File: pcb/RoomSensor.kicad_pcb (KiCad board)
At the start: 2 copper layers, 82 x 36.5 mm, 75 parts, among them J1 FH34SRJ-24S-0.5SH50, J2 USB_C_Receptacle_PowerOnly_6P, J3 programming, J4 Conn_01x04_Pin, J5 Conn_01x04_Pin, J6 Conn_01x02_Pin, Q1 SI1308EDL-T1-GE3, Q2 AO3401A, Q3 ALS-PT19-315C/L177/TR8, SW1 SW_Push, U1 ESP32-WROOM-32D, U2 DW01-P, U3 CEG8205A, U4 RT9080-33GJ5, U5 TP4056, U6 SCD40-D-R1, U7 SHT31-DIS, U8 BME680

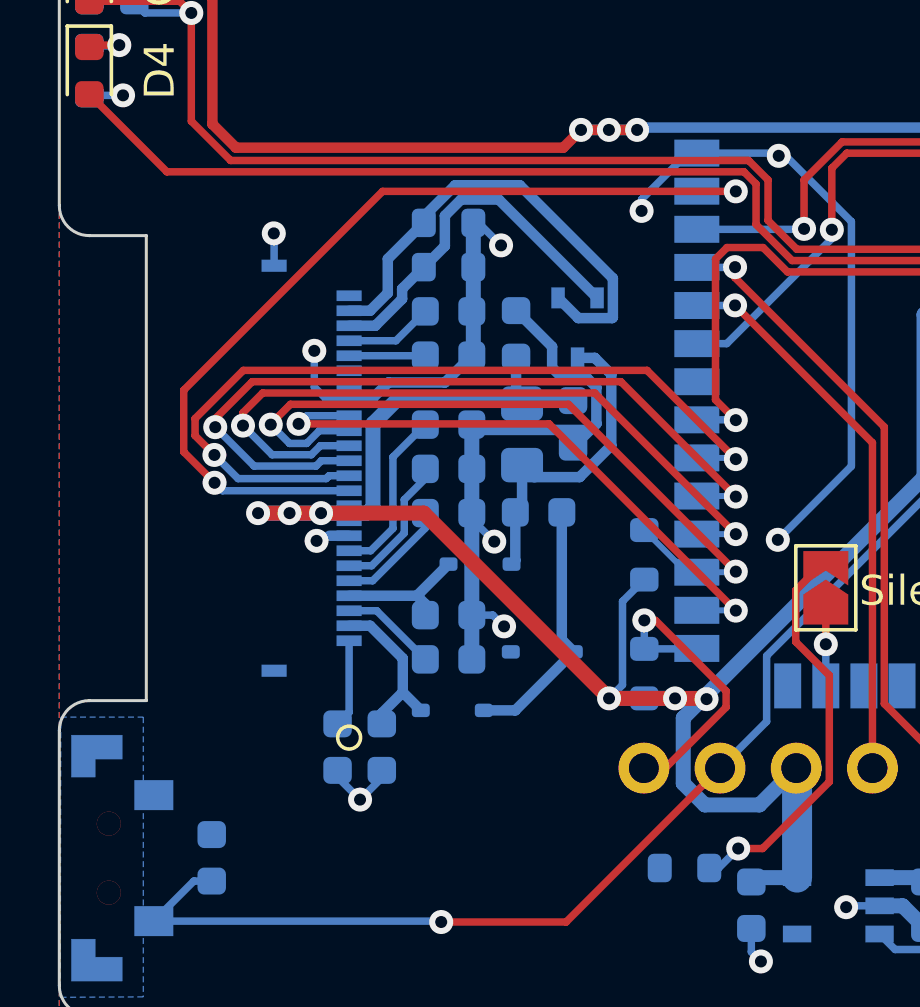
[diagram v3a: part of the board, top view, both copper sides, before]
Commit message: Move epd connector and fix net
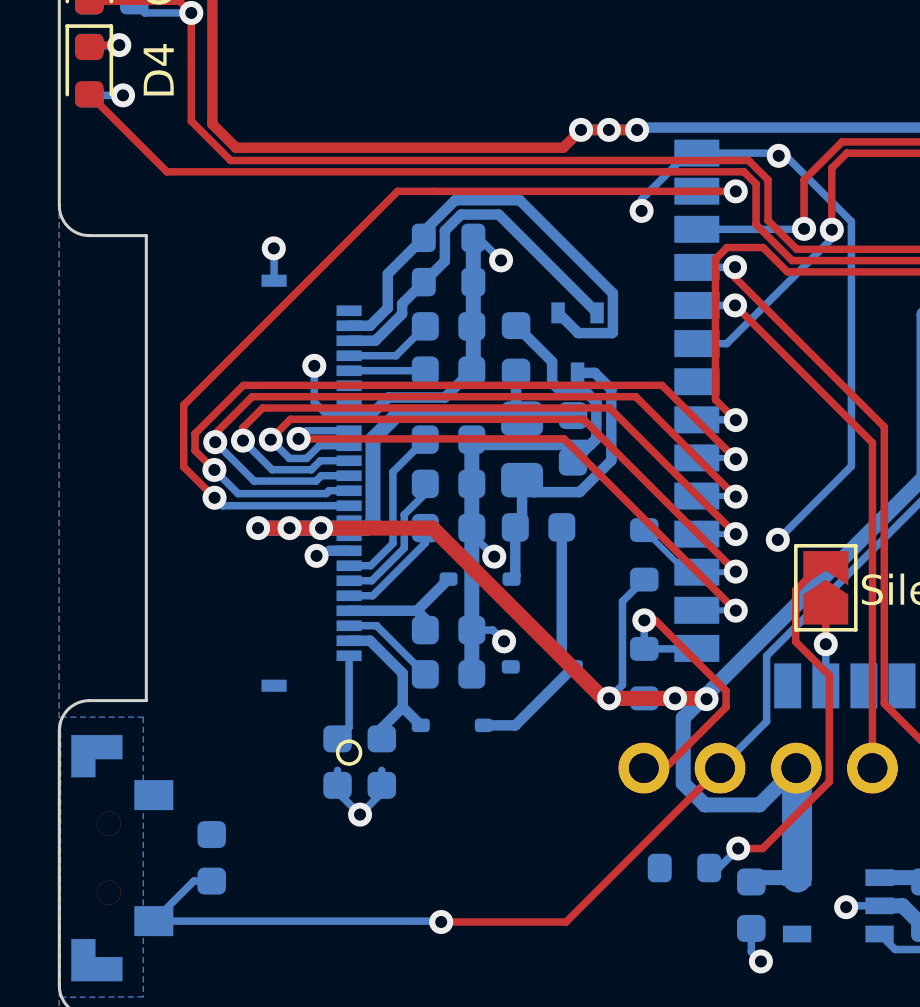
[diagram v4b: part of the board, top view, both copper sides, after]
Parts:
- moved C1 0.50 mm to (7.28, 28.1)
- moved C10 0.50 mm to (11.0, 13.5)
- moved C11 0.50 mm to (14.0, 20.2)
- moved C12 0.50 mm to (13.2, 14.3)
- moved C2 0.50 mm to (11.0, 25.1)
- moved C3 0.50 mm to (11.0, 20.2)
- moved C4 0.50 mm to (11.0, 17.3)
- moved C5 0.50 mm to (15.1, 17.3)
- moved C6 0.50 mm to (11.0, 15.0)
- moved C7 0.50 mm to (8.75, 28.1)
- moved C8 0.50 mm to (11.0, 23.6)
- moved C9 0.50 mm to (11.0, 18.8)
- moved D1 0.50 mm to (14.1, 24.9)
- moved D2 0.50 mm to (11.1, 26.8)
- moved D3 0.50 mm to (12.0, 21.9)
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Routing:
- removed copper zone on F.Cu, net -BATT
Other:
- board text added: "RoomSensor V2023.08.02 by wirmo aka enwi"
- board text removed: "RoomSensor V2023.07.30 by wirmo aka enwi"
